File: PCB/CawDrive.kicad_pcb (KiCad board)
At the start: 4 copper layers, 50 x 42 mm, 109 parts, among them CN2 WAFER-SH1.0-6PWB, CN3 WAFER-SH1.0-4PWB, Q10 TPH3R704PL, Q11 TPH3R704PL, Q12 TPH3R704PL, Q7 TPH3R704PL, Q8 TPH3R704PL, Q9 TPH3R704PL, U1 TJA1051T/3/1J, U10 WAFER-SH1.0-2PWB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

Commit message: 更新采样电阻精度，重新生成BOM
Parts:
- R1, R20: value 10k 1% -> 10k 0.1%
- R12: value 3k 1% -> 3k 0.1%
- R21: value NTC -> 10k NTC
- R8: value 75k 1% -> 75k 0.1%

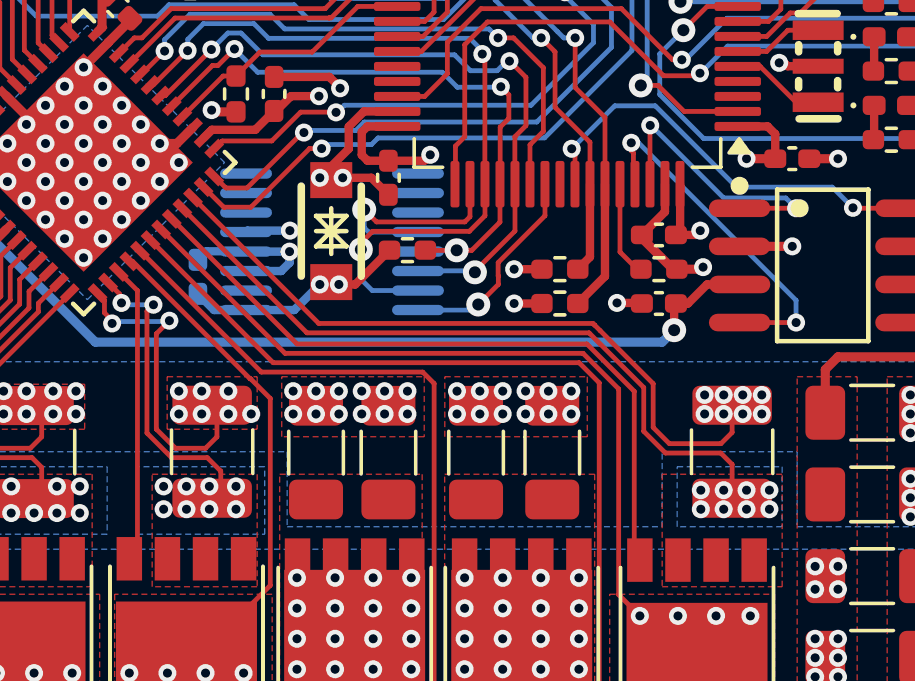
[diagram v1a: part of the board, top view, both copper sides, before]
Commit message: 优化电流采样布线
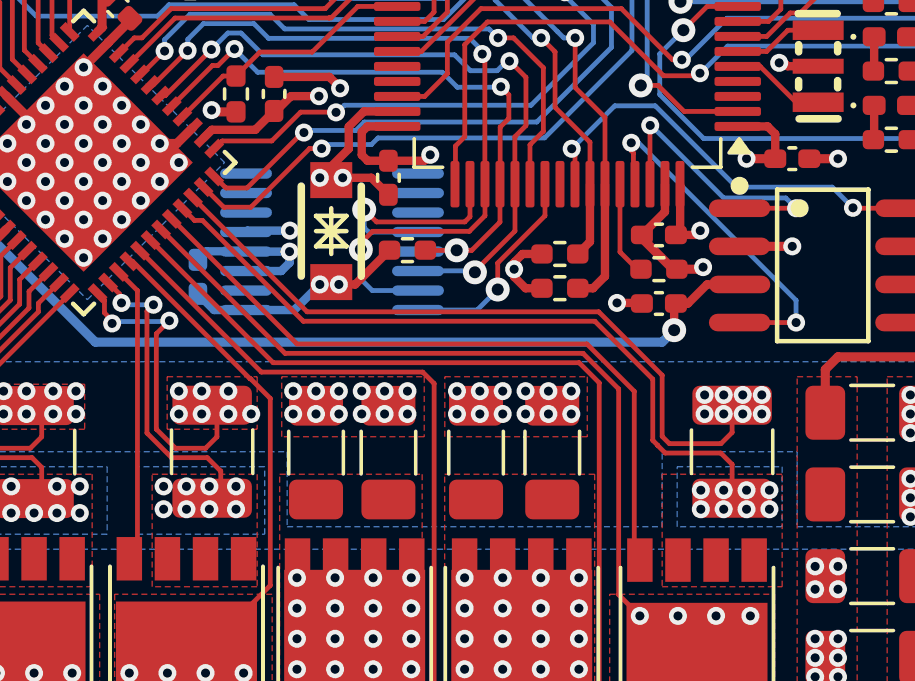
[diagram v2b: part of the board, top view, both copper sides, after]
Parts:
- moved R5 0.51 mm to (148.6, 89.4)
- moved R6 0.51 mm to (148.6, 90.6)
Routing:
- net +3.3V: track 54.2 -> 55.0 mm, vias 22 -> 21
- net /I2C1_SCL: track 21.7 -> 21.2 mm

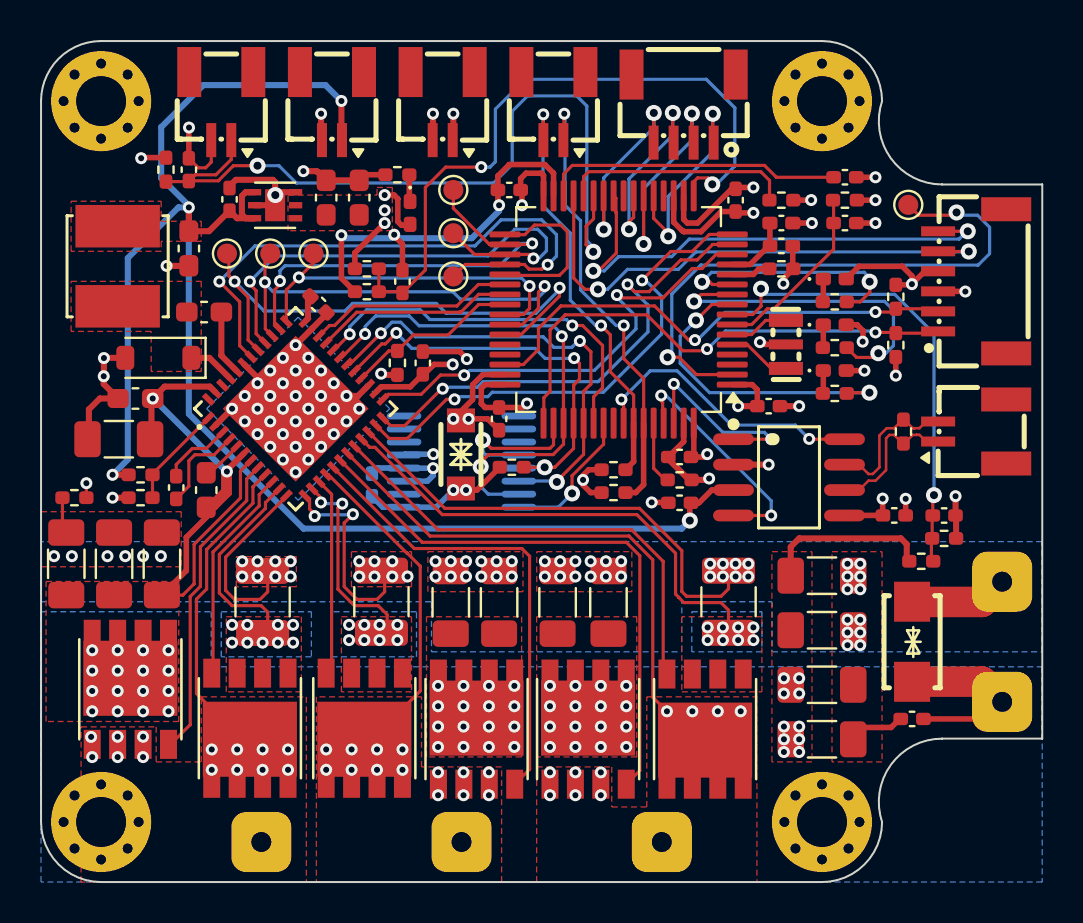
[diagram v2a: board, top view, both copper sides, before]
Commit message: 优化ADC采样布线
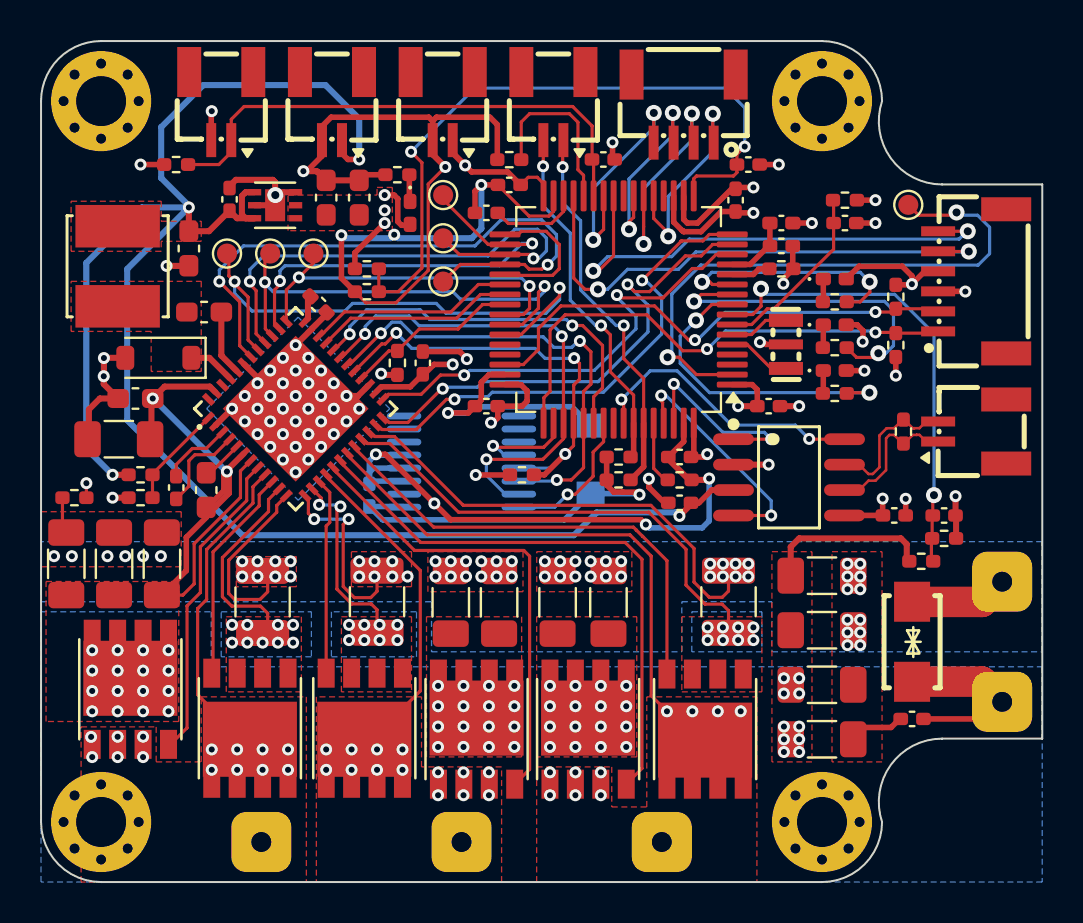
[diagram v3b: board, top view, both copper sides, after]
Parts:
- D5: moved to B.Cu
- moved C1 20.7 mm to (148.1, 73.9), turned to 180 degrees
- moved C12 18.2 mm to (155.3, 74.2), turned to 180 degrees
- moved C9 18.0 mm to (142.2, 76.6), turned to 0 degrees
- moved R25 13.7 mm to (143.4, 73.9), turned to 180 degrees
- moved D5 6.48 mm to (147.4, 88.9)
- moved C5 0.90 mm to (142.2, 86.2), turned to 180 degrees
- moved R5 0.68 mm to (148.8, 88.8)
- moved R6 0.68 mm to (148.8, 89.9)
- moved R16 0.64 mm to (144.0, 89.7)
- moved TP2 0.57 mm to (140.1, 77.9)
- moved TP3 0.57 mm to (140.1, 80.0)
- moved TP1 0.57 mm to (140.1, 75.7)
- moved R1 0.57 mm to (126.7, 74.2), turned to 180 degrees
- moved C18 0.52 mm to (136.4, 90.7)
- moved C4 0.25 mm to (143.4, 75.2)
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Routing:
- net GND: track 90.4 -> 138.1 mm, vias 68 -> 67
- net /ADC2_IN9: track 39.3 -> 25.5 mm, vias 2 -> 0
- net +3.3V: track 55.0 -> 66.9 mm, vias 21 -> 19
- net Net-(U8-VCAP_1): track 15.0 -> 4.53 mm
- net +5V: track 81.2 -> 90.2 mm
- net /I2C1_SDA: track 22.8 -> 19.1 mm
- net /I2C1_SCL: track 21.2 -> 17.7 mm
- net Net-(U8-PB2): track 11.5 -> 8.85 mm
- net /ENCODER_CAL_EN: track 7.30 -> 4.76 mm
- net /TIM1_BKIN: track 8.45 -> 6.40 mm
- net /SPI3_SCK: track 25.8 -> 24.2 mm
- net /SPI1_NSS: track 10.0 -> 11.5 mm
- net GND1: track 52.3 -> 51.2 mm
- net /TIM1_CH3N: track 29.7 -> 30.6 mm
- net /SPI3_MISO: track 21.1 -> 22.0 mm
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
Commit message: 优化走线
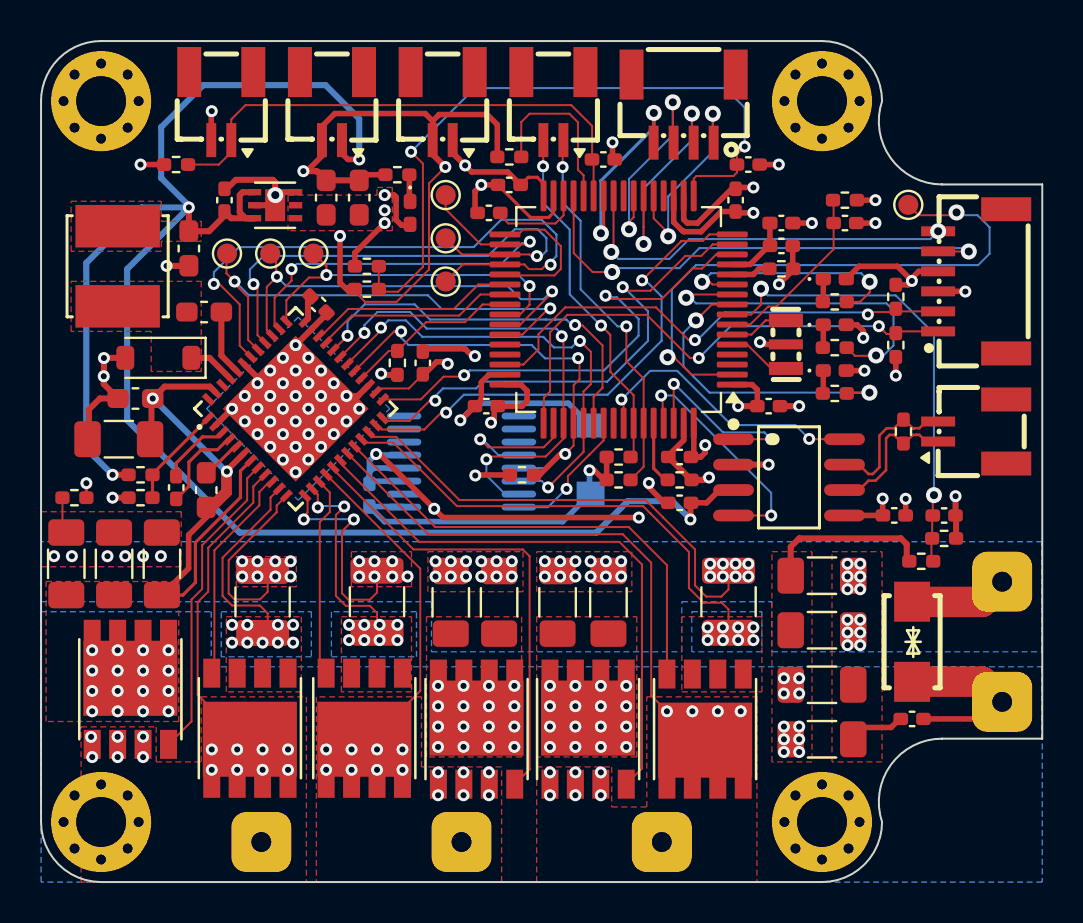
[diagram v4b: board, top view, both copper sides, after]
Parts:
- moved C7 0.26 mm to (129.2, 75.9)
- moved R25 0.14 mm to (143.4, 73.8)
- moved TP1 0.13 mm to (140.2, 75.7)
- moved TP2 0.13 mm to (140.2, 77.9)
- moved TP3 0.13 mm to (140.2, 80.0)
- moved R20 0.13 mm to (136.3, 79.2)
- moved R21 0.13 mm to (136.3, 80.4)
- moved C9 0.13 mm to (142.4, 76.6)
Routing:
- net GND: track 138.1 -> 121.9 mm, vias 67 -> 66
- net /USART3_RX: track 25.3 -> 19.9 mm
- net /TIM1_CH3: track 27.8 -> 24.5 mm
- net +3.3V: track 66.9 -> 63.8 mm
- net /ADC1_IN0: track 23.0 -> 24.4 mm
- net /USART3_TX: track 26.4 -> 25.1 mm
- net GND1: track 51.2 -> 52.4 mm
- net /SPI1_MOSI: track 9.93 -> 11.0 mm
- net /SPI1_NSS: track 11.5 -> 10.5 mm
- net /ENCODER_CAL_EN: track 4.76 -> 5.58 mm
- net /DRV_STA: track 16.6 -> 17.3 mm
- net /DRV8323RSRGZR/SPB: track 9.92 -> 10.5 mm
- net /TIM1_CH2: track 22.1 -> 21.6 mm

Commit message: 更新Gerber
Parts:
- added G***: LOGO, Rick_Logo:guaik_logo_black_6x6, B.Cu at (155.8, 91.6)
- moved C19 14.3 mm to (156.7, 80.1), turned to 90 degrees
- moved C11 1.14 mm to (157.0, 77.1)
- moved L1 1.14 mm to (157.0, 75.9)
- moved R12 1.14 mm to (165.1, 91.7)
- moved R24 1.14 mm to (157.0, 78.2)
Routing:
- net GND: track 121.9 -> 125.5 mm, vias 66 -> 70
- net /USART3_RX: track 19.9 -> 22.8 mm
- net +3.3V: track 63.8 -> 62.0 mm
- net +3.3VA: track 3.34 -> 4.53 mm
- net Net-(U8-VSSA): track 1.97 -> 2.79 mm
- net /TIM1_CH2N: track 25.9 -> 25.2 mm
- net /ADC1_IN10: track 23.2 -> 22.5 mm
- net /RESET: track 9.04 -> 9.59 mm
- net /TIM1_CH3N: track 31.1 -> 30.5 mm
- net GND1: track 52.4 -> 52.5 mm, vias 67 -> 66

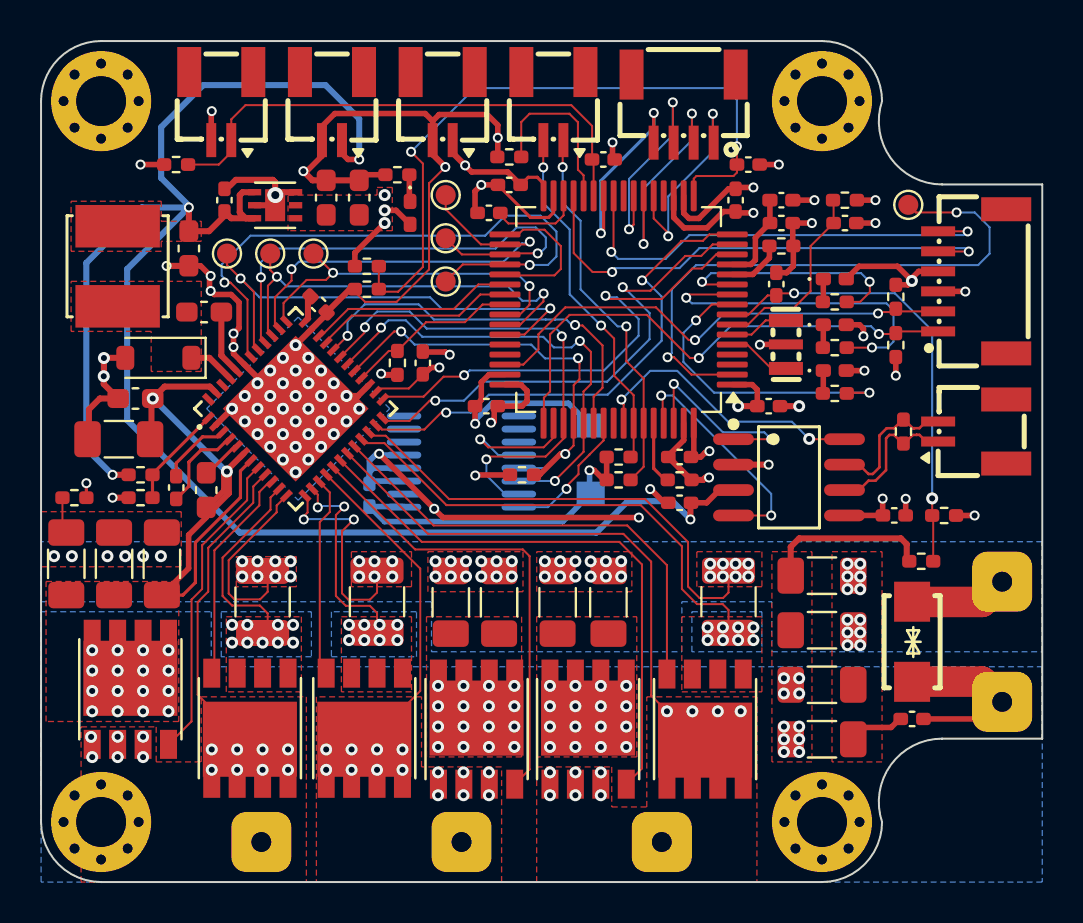
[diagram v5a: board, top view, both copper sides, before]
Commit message: PCB走线优化
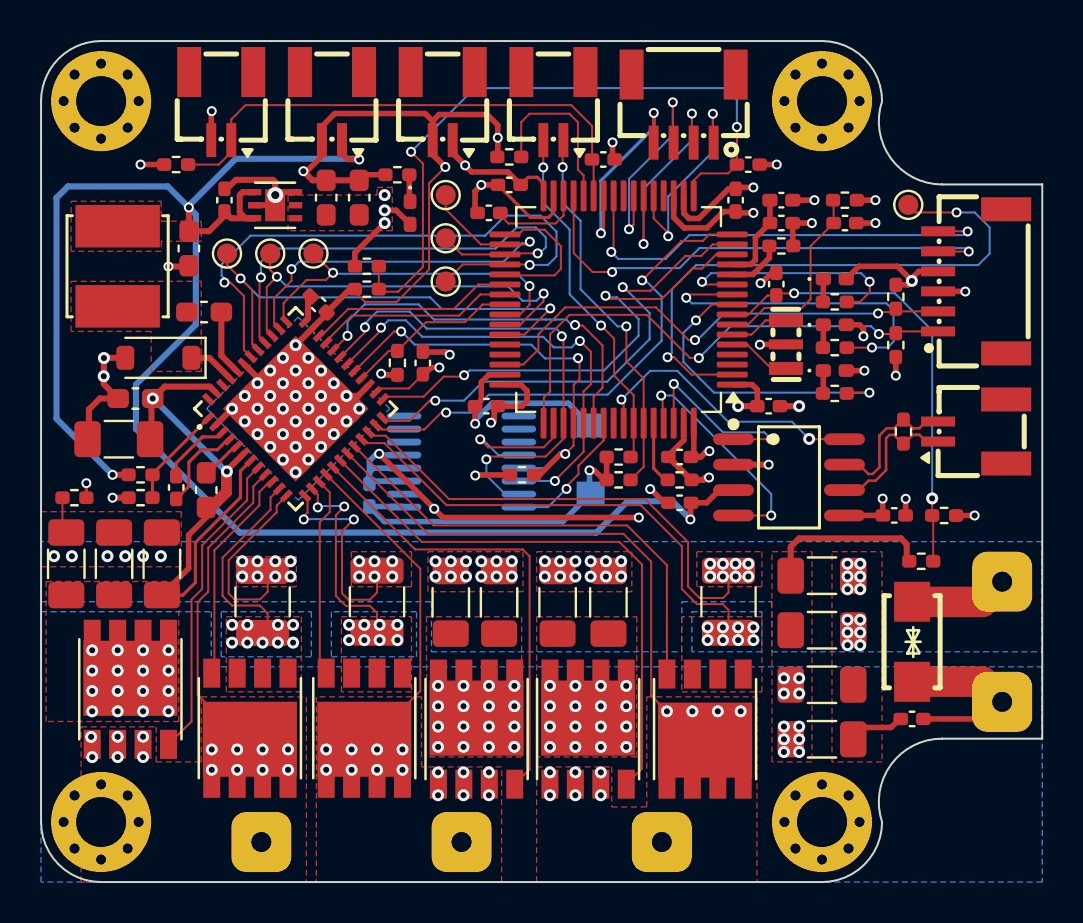
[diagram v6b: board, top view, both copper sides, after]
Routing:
- net GND: track 125.5 -> 117.2 mm, vias 70 -> 67
- net +5V: track 90.5 -> 86.8 mm

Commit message: 优化PCB
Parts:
- removed D5: SMF6.0CA_C2836402, Rick_Diode:SMF6.0CA_SOD-123FL_L2.8-W1.8-LS3.7-BI
- removed the G*** at (155.8, 91.6)
- removed R22: 5mΩ 1%, Resistor_SMD:R_1210_3225Metric_Pad1.30x2.65mm_HandSolder
- added G***: LOGO, Rick_Logo:guaik_logo_black_7x7, B.Cu at (155.3, 92.1)
- added REF**: OSHW-Logo_5.7x6mm_SilkScreen, Symbol:OSHW-Logo_5.7x6mm_SilkScreen, F.Cu at (153.2, 95.2)
- moved R25 16.8 mm to (160.1, 74.8), turned to 0 degrees
- moved C9 14.8 mm to (157.0, 74.2), turned to 180 degrees
- moved R20 11.7 mm to (141.0, 89.9)
- moved R21 11.7 mm to (141.0, 91.1)
- moved R5 5.34 mm to (144.0, 91.1)
- moved TP3 4.54 mm to (135.9, 78.6)
- moved TP1 2.93 mm to (140.5, 78.6)
- moved R23 2.90 mm to (149.2, 91.1), turned to 0 degrees
- moved R6 2.67 mm to (146.4, 91.1), turned to 0 degrees
- moved C12 2.25 mm to (157.0, 75.7)
- moved TP2 2.17 mm to (138.2, 78.6)
- moved D4 2.04 mm to (140.5, 76.5)
- moved R7 2.03 mm to (139.8, 74.7)
- moved C7 1.92 mm to (131.1, 76.2)
- moved C34 1.91 mm to (136.1, 75.9)
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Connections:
- C12 pad 2: /ADC3_IN3 -> /ADC3_IN2
- Q12 pad 1: /DRV8323RSRGZR/SPC -> GND1
- Q12 pad 2: /DRV8323RSRGZR/SPC -> GND1
- Q12 pad 3: /DRV8323RSRGZR/SPC -> GND1
- R20 pad 1: /ADC3_IN3 -> /ADC3_IN2
- R21 pad 2: /ADC3_IN3 -> /ADC3_IN2
- U7 pad 21: /DRV8323RSRGZR/SPC -> GND1
- U7 pad 23: /ADC3_IN2 -> unconnected-(U7-SOC-Pad23)
- U8 pad 17: /ADC3_IN3 -> unconnected-(U8-PA3-Pad17)
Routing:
- net +5V: track 86.8 -> 26.5 mm, vias 4 -> 5
- net GND: track 117.2 -> 68.5 mm, vias 67 -> 48
- net /ADC3_IN3: track 34.0 -> 0.00 mm, vias 2 -> 0
- net /DRV8323RSRGZR/SPC: track 24.0 -> 0.00 mm, vias 8 -> 0
- net +3.3V: track 62.0 -> 52.7 mm, vias 19 -> 24
- net /I2C1_SCL: track 17.6 -> 25.8 mm
- net Net-(U8-VCAP_1): track 4.47 -> 12.1 mm, vias 0 -> 2
- net /ADC3_IN2: track 25.1 -> 31.9 mm
- net /SPI1_MISO: track 11.3 -> 4.84 mm, vias 2 -> 0
- net /SPI1_MOSI: track 11.0 -> 4.61 mm, vias 2 -> 0
- net /I2C1_SDA: track 19.1 -> 25.1 mm
- net Net-(U8-PC13): track 29.5 -> 23.7 mm
- net /SPI1_NSS: track 10.5 -> 4.74 mm, vias 2 -> 0
- net Net-(U8-PB2): track 8.72 -> 14.1 mm, vias 0 -> 2
- net /SPI1_SCK: track 10.8 -> 5.57 mm, vias 2 -> 0
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- added copper zone on In2.Cu, net +5V
- removed copper zone on B.Cu, net /DRV8323RSRGZR/SPC
- removed copper zone on F.Cu, net /DRV8323RSRGZR/SPC

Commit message: 优化PCB
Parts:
- moved R17 0.25 mm to (138.0, 83.6)
- moved C32 0.13 mm to (139.2, 83.6)
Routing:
- net /TIM1_CH1: track 20.6 -> 18.9 mm
- net /SPI3_SCK: track 23.4 -> 24.9 mm
- net /TIM1_CH3N: track 26.9 -> 27.9 mm
- net /TIM1_CH2N: track 24.4 -> 25.2 mm
- net GND: track 68.5 -> 69.1 mm, vias 48 -> 49
- net /TIM1_CH1N: track 21.3 -> 20.7 mm
- net /MCU_STA: track 13.9 -> 13.3 mm
- net /SPI3_MOSI: track 21.0 -> 21.5 mm
- net +3.3V: track 52.7 -> 52.8 mm, vias 24 -> 23
